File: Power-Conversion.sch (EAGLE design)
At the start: 99 parts, among them T3 FDN340P, U1 ATMEGA328P_TQFP, U2 LM1085IS-3.3, U3 LM1085IS-3.3, U4 PCA9685, U5 FT232RLSSOP

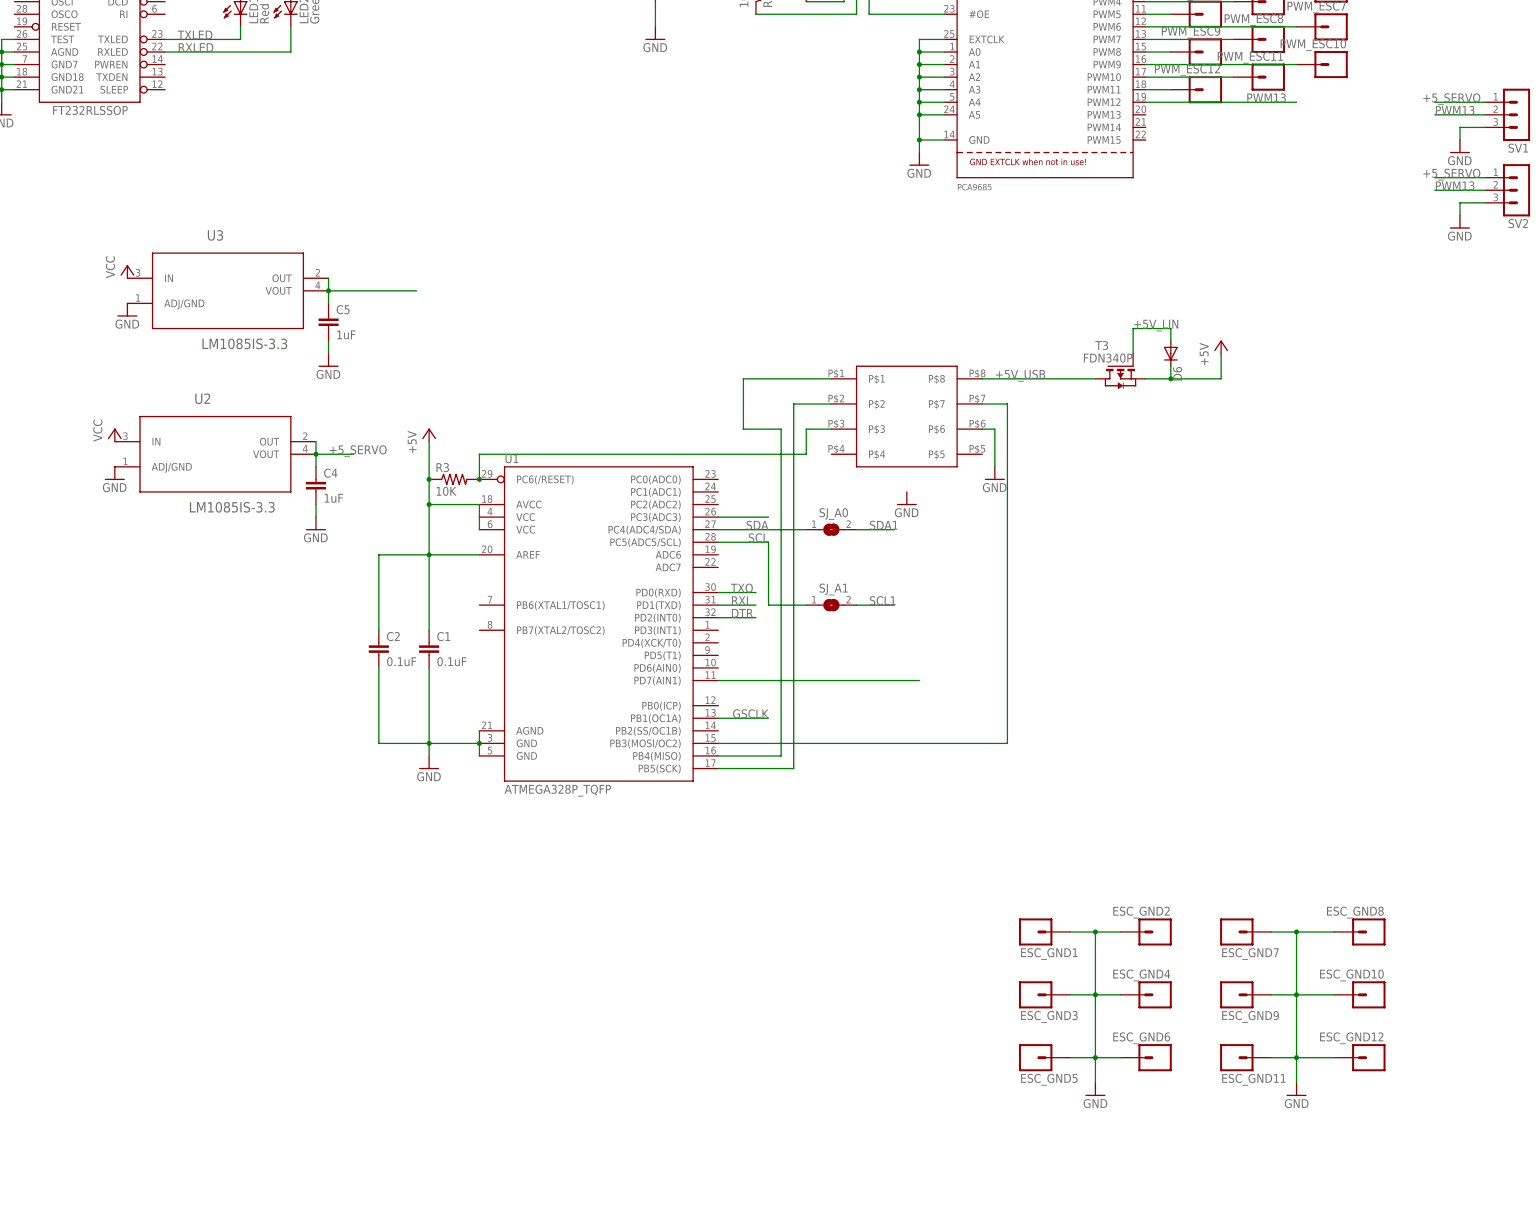
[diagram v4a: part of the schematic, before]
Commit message: Switched from a linear regulator to a buck regulator
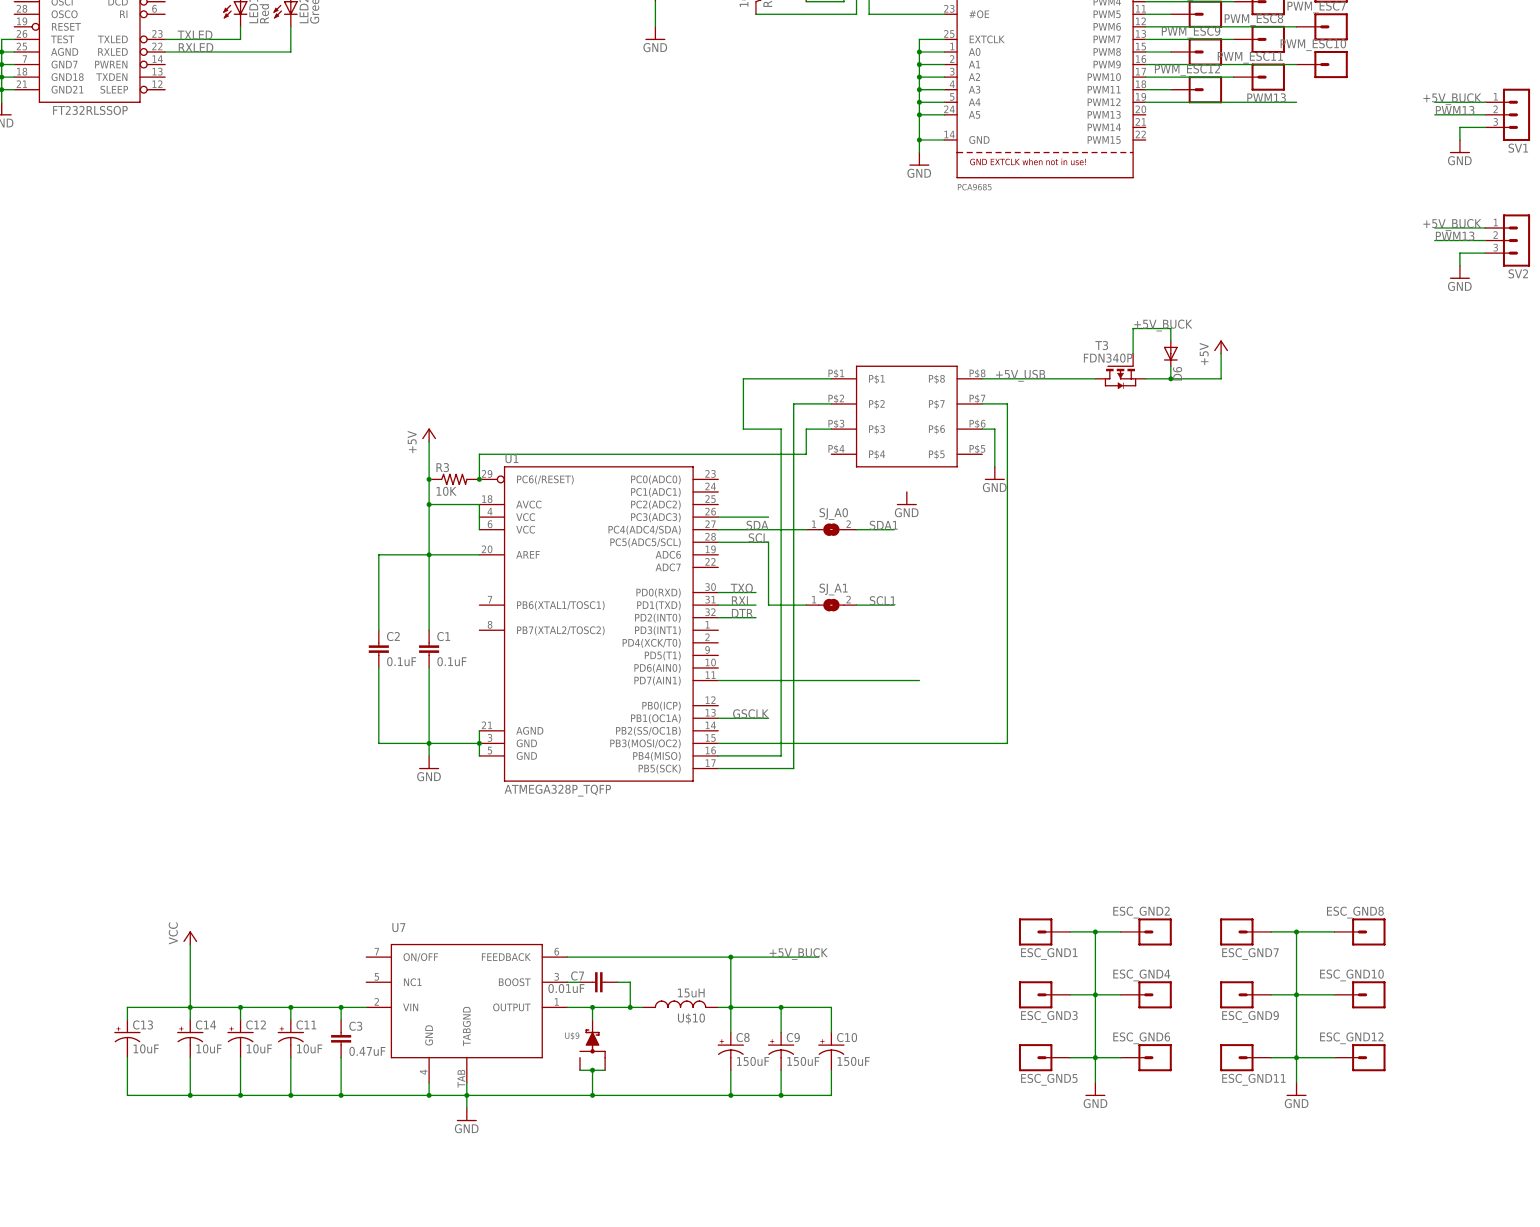
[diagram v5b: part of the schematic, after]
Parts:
- removed C4, C5: 1uF, SparkFun-Capacitors:0.1UF-25V(+80/-20%)(0603)
- removed U2, U3: LM1085IS-3.3, PowerComponents:LM1085IS-3.3
- added C10, C8, C9: 150uF, PowerComponents:C-TANTALUM(10UF_150UF)
- added C11, C12, C13, C14: 10uF, PowerComponents:C-TANTALUM(10UF_150UF)
- added C3: 0.47uF, SparkFun-Capacitors:CAP0805
- added C7: 0.01uF, SparkFun-Passives:CAP0603-CAP
- added U$10: 15uH, DiscreteComponents:HCMA1305
- added U$9: SWITCHMODE_SCHOTTKY, PowerComponents:SWITCHMODE_SCHOTTKY
- added U7: LM2678, PowerComponents:LM2678
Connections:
- removed net +5V_LIN: C5.1, D6.A, T3.G, U3.OUT, U3.VOUT
- removed net +5_SERVO: C4.1, SV1.1, SV2.1, U2.OUT, U2.VOUT
- new net +5V_BUCK: C10.+, C8.+, C9.+, D6.A, SV1.1, SV2.1, T3.G, U$10.2, U7.FEEDBACK
- new net N$25: C7.1, U7.BOOST
- new net N$36: C7.2, U$10.1, U$9.P$4, U7.OUTPUT
- net GND: now also C10.-, C11.-, C12.-, C13.-, C14.-, C3.2, C8.-, C9.-, U$9.P$1, U$9.P$3, U7.GND, U7.TABGND; no longer C4.2, C5.2, U2.ADJ/GND, U3.ADJ/GND
- net VCC: now also C11.+, C12.+, C13.+, C14.+, C3.1, U7.VIN; no longer U2.IN, U3.IN
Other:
- moved on the sheet: SV2

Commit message: Fixed most suggestions from Michael.  Also added some cosmetic changes
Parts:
- removed SJ_A0, SJ_A1: (no value), microbuilder:SOLDERJUMPERREFLOW_NOPASTE
- added C4: 0.1uF, SparkFun-Capacitors:0.1UF-25V(+80/-20%)(0603)
- added R9: 10k, SparkFun:RESISTOR0402-RES
- added SCL, SDA: 0, rcl:R-EU_R0603
- C3: device SparkFun-Capacitors:CAP0805 -> rcl:C-EUC0603
- R4, R5: device SparkFun:RESISTOR0402-RES -> resistor:R-US_R0603
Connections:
- new net N$37: C4.1, U5.3V3OUT
- new net N$38: R9.1, U5.RESET
- net +5V: now also R9.2
- net GND: now also C4.2
- net SCL: now also SCL.1; no longer SJ_A1.1
- net SCL1: now also SCL.2; no longer SJ_A1.2
- net SDA: now also SDA.1; no longer SJ_A0.1
- net SDA1: now also SDA.2; no longer SJ_A0.2
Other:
- moved on the sheet: C1, C10, C11, C12, C13, C14, C2, C3, C6, C7, C8, C9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

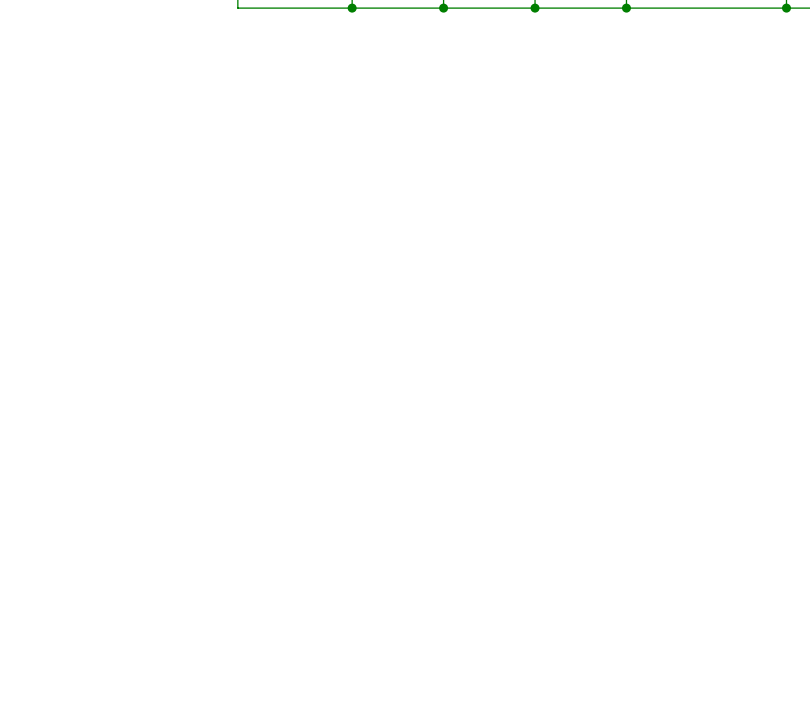
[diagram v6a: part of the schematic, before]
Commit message: Added debugging pins and more silk screen
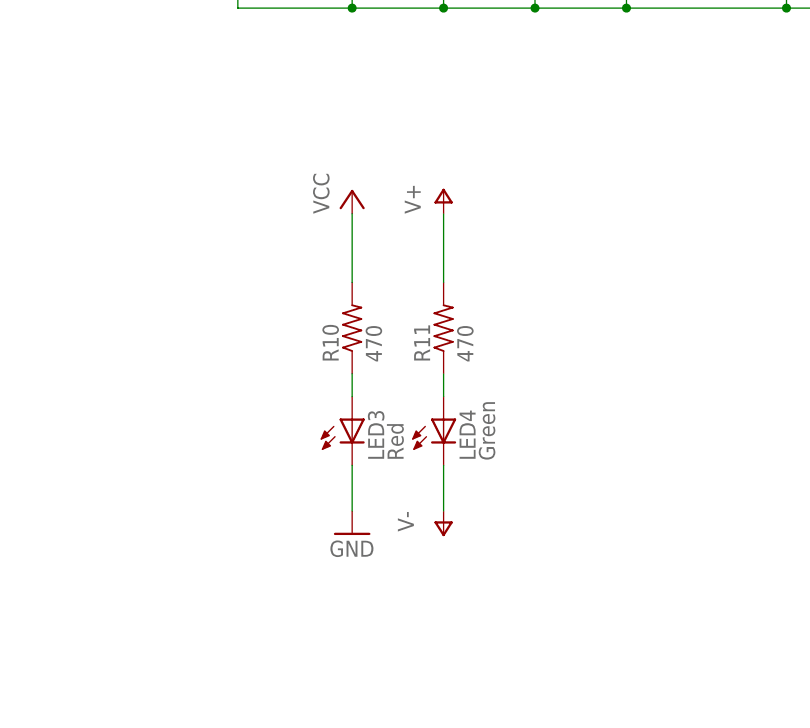
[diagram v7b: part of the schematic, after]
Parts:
- added LED3: Red, SparkFun:LED0603
- added LED4: Green, SparkFun:LED0603
- added R10, R11: 470, resistor:R-US_R0603
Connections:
- new net N$39: LED3.A, R10.1
- new net N$40: LED4.A, R11.1
- net GND: now also LED3.C
- net V+: now also R11.2
- net V-: now also LED4.C
- net VCC: now also R10.2
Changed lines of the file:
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@@
 <part name="GND14" library="SparkFun" deviceset="GND" device=""/>
 <part name="R9" library="SparkFun" deviceset="RESISTOR" device="0402-RES" value="10k"/>
+<part name="R10" library="resistor" deviceset="R-US_" device="R0603" value="470"/>
+<part name="R11" library="resistor" deviceset="R-US_" device="R0603" value="470"/>
+<part name="LED3" library="SparkFun" deviceset="LED" device="0603" value="Red"/>
+<part name="LED4" library="SparkFun" deviceset="LED" device="0603" value="Green"/>
+<part name="P+8" library="supply1" deviceset="VCC" device=""/>
+<part name="P+9" library="supply1" deviceset="V+" device=""/>
+<part name="P-8" library="supply1" deviceset="V-" device=""/>
+<part name="GND18" library="supply1" deviceset="GND" device=""/>
 </parts>
 <sheets>
@@
 <instance part="GND14" gate="1" x="60.96" y="477.52"/>
 <instance part="R9" gate="G$1" x="76.2" y="482.6" rot="R180"/>
+<instance part="R10" gate="G$1" x="228.6" y="172.72" rot="R90"/>
+<instance part="R11" gate="G$1" x="238.76" y="172.72" rot="R90"/>
+<instance part="LED3" gate="G$1" x="228.6" y="162.56"/>
+<instance part="LED4" gate="G$1" x="238.76" y="162.56"/>
+<instance part="P+8" gate="VCC" x="228.6" y="187.96"/>
+<instance part="P+9" gate="1" x="238.76" y="187.96"/>
+<instance part="P-8" gate="1" x="238.76" y="149.86"/>
+<instance part="GND18" gate="1" x="228.6" y="149.86"/>
 </instances>
 <busses>
@@
 <wire x1="53.34" y1="137.16" x2="45.72" y2="137.16" width="0.1524" layer="91"/>
 </segment>
+<segment>
+<pinref part="P+9" gate="1" pin="V+"/>
+<pinref part="R11" gate="G$1" pin="2"/>
+<wire x1="238.76" y1="185.42" x2="238.76" y2="177.8" width="0.1524" layer="91"/>
+</segment>
 </net>
 <net name="V-" class="0">
@@
 <pinref part="P-7" gate="1" pin="V-"/>
 <wire x1="53.34" y1="132.08" x2="45.72" y2="132.08" width="0.1524" layer="91"/>
+</segment>
+<segment>
+<pinref part="LED4" gate="G$1" pin="C"/>
+<pinref part="P-8" gate="1" pin="V-"/>
+<wire x1="238.76" y1="157.48" x2="238.76" y2="152.4" width="0.1524" layer="91"/>
 </segment>
 </net>
@@
 <wire x1="228.6" y1="238.76" x2="228.6" y2="226.06" width="0.1524" layer="91"/>
 </segment>
+<segment>
+<pinref part="P+8" gate="VCC" pin="VCC"/>
+<pinref part="R10" gate="G$1" pin="2"/>
+<wire x1="228.6" y1="185.42" x2="228.6" y2="177.8" width="0.1524" layer="91"/>
+</segment>
 </net>
 <net name="GND" class="0">
@@
 <wire x1="60.96" y1="482.6" x2="60.96" y2="480.06" width="0.1524" layer="91"/>
 </segment>
+<segment>
+<pinref part="LED3" gate="G$1" pin="C"/>
+<pinref part="GND18" gate="1" pin="GND"/>
+<wire x1="228.6" y1="157.48" x2="228.6" y2="152.4" width="0.1524" layer="91"/>
+</segment>
 </net>
 <net name="SCL" class="0">
@@
 </segment>
 </net>
+<net name="N$39" class="0">
+<segment>
+<wire x1="228.6" y1="167.64" x2="228.6" y2="165.1" width="0.1524" layer="91"/>
+<pinref part="R10" gate="G$1" pin="1"/>
+<pinref part="LED3" gate="G$1" pin="A"/>
+</segment>
+</net>
+<net name="N$40" class="0">
+<segment>
+<wire x1="238.76" y1="167.64" x2="238.76" y2="165.1" width="0.1524" layer="91"/>
+<pinref part="R11" gate="G$1" pin="1"/>
+<pinref part="LED4" gate="G$1" pin="A"/>
+</segment>
+</net>

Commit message: Fixed a few silkscrean problems
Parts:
- renumbered ESC_GND1 to G1, ESC_GND10 to G10, ESC_GND11 to G11, ESC_GND12 to G12, ESC_GND2 to G2, ESC_GND3 to G3, ESC_GND4 to G4, ESC_GND5 to G5, ESC_GND6 to G6, ESC_GND7 to G7, ESC_GND8 to G8, ESC_GND9 to G9, PWM_ESC1 to P1, PWM_ESC10 to P10, PWM_ESC11 to P11, PWM_ESC12 to P12, PWM_ESC2 to P2, PWM_ESC3 to P3, PWM_ESC4 to P4, PWM_ESC5 to P5, PWM_ESC6 to P6, PWM_ESC7 to P7, PWM_ESC8 to P8, PWM_ESC9 to P9
